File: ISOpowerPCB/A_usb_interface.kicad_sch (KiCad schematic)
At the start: 10 parts, among them J19 USB_B_Mini, U12 CH340C

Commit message: added documentation for component selection
Completed footprint association & added documentation re Netclasses. Need to update netclasses in schematic settings before moving to PCB layout.
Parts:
- J19: footprint (none) -> Connector_USB:USB_Mini-B_Lumberg_2486_01_Horizontal
- TP7, TP8: footprint (none) -> TestPoint:TestPoint_Pad_D1.5mm
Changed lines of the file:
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@@
       (effects (font (size 1.27 1.27)) (justify left))
     )
-    (property "Footprint" "" (id 2) (at 161.29 77.47 0)
+    (property "Footprint" "TestPoint:TestPoint_Pad_D1.5mm" (id 2) (at 161.29 77.47 0)
       (effects (font (size 1.27 1.27)) hide)
     )
@@
       (effects (font (size 1.27 1.27)) (justify left))
     )
-    (property "Footprint" "" (id 2) (at 120.65 77.47 0)
+    (property "Footprint" "TestPoint:TestPoint_Pad_D1.5mm" (id 2) (at 120.65 77.47 0)
       (effects (font (size 1.27 1.27)) hide)
     )
@@
       (effects (font (size 1.27 1.27)) (justify right))
     )
-    (property "Footprint" "" (id 2) (at 177.8 93.98 0)
+    (property "Footprint" "Connector_USB:USB_Mini-B_Lumberg_2486_01_Horizontal" (id 2) (at 177.8 93.98 0)
       (effects (font (size 1.27 1.27)) hide)
     )

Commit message: PCB Layouts
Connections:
- net 5V_CH340 renamed 5V_IN
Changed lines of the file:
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@@
-    (stroke (width 0) (type default) (color 0 0 0 0))
-  )
-  (wire (pts (xy 27.94 22.86) (xy 39.37 22.86))
     (stroke (width 0) (type default) (color 0 0 0 0))
   )
@@
     (stroke (width 0) (type default) (color 0 0 0 0))
   )
-  (wire (pts (xy 27.94 30.48) (xy 39.37 30.48))
-    (stroke (width 0) (type default) (color 0 0 0 0))
-  )
   (wire (pts (xy 115.57 77.47) (xy 119.38 77.47))
     (stroke (width 0) (type default) (color 0 0 0 0))
@@
   )
   (wire (pts (xy 156.21 123.19) (xy 156.21 96.52))
-    (stroke (width 0) (type default) (color 0 0 0 0))
-  )
-  (wire (pts (xy 27.94 26.67) (xy 39.37 26.67))
     (stroke (width 0) (type default) (color 0 0 0 0))
   )
@@
     (effects (font (size 2 2)) (justify left bottom))
   )
-  (label "3V3_BUS" (at 29.21 26.67 0)
-    (effects (font (size 1.27 1.27)) (justify left bottom))
-  )
-  (global_label "5V_CH340" (shape output) (at 39.37 22.86 0) (fields_autoplaced)
+  (hierarchical_label "TxD_A" (shape output) (at 92.71 115.57 180)
+    (effects (font (size 1.27 1.27)) (justify right))
+  )
+  (hierarchical_label "5V_IN" (shape input) (at 132.08 62.23 90)
     (effects (font (size 1.27 1.27)) (justify left))
-    (property "Intersheet References" "${INTERSHEET_REFS}" (id 0) (at 51.2779 22.7806 0)
-      (effects (font (size 1.27 1.27)) (justify left) hide)
-    )
-  )
-  (global_label "3V3_CH340" (shape output) (at 39.37 26.67 0) (fields_autoplaced)
+  )
+  (hierarchical_label "GND" (shape passive) (at 132.08 110.49 270)
+    (effects (font (size 1.27 1.27)) (justify right))
+  )
+  (hierarchical_label "5V_IN" (shape input) (at 113.03 101.6 90)
     (effects (font (size 1.27 1.27)) (justify left))
-    (property "Intersheet References" "${INTERSHEET_REFS}" (id 0) (at 52.4874 26.5906 0)
-      (effects (font (size 1.27 1.27)) (justify left) hide)
-    )
-  )
-  (global_label "5V_CH340" (shape input) (at 132.08 62.23 90) (fields_autoplaced)
-    (effects (font (size 1.27 1.27)) (justify left))
-    (property "Intersheet References" "${INTERSHEET_REFS}" (id 0) (at 132.0006 50.3221 90)
-      (effects (font (size 1.27 1.27)) (justify left) hide)
-    )
-  )
-  (global_label "5V_CH340" (shape input) (at 113.03 101.6 90) (fields_autoplaced)
-    (effects (font (size 1.27 1.27)) (justify left))
-    (property "Intersheet References" "${INTERSHEET_REFS}" (id 0) (at 112.9506 89.6921 90)
-      (effects (font (size 1.27 1.27)) (justify left) hide)
-    )
-  )
-  (hierarchical_label "TxD_A" (shape output) (at 92.71 115.57 180)
-    (effects (font (size 1.27 1.27)) (justify right))
-  )
-  (hierarchical_label "5V_IN" (shape input) (at 27.94 22.86 180)
-    (effects (font (size 1.27 1.27)) (justify right))
   )
   (hierarchical_label "USB_VOUT" (shape output) (at 170.18 87.63 180)
     (effects (font (size 1.27 1.27)) (justify right))
   )
-  (hierarchical_label "3V3_IN" (shape input) (at 27.94 26.67 180)
+  (hierarchical_label "GND" (shape passive) (at 198.12 120.65 270)
     (effects (font (size 1.27 1.27)) (justify right))
   )
@@
     (effects (font (size 1.27 1.27)) (justify right))
   )
-  (hierarchical_label "GND" (shape passive) (at 27.94 30.48 180)
+  (hierarchical_label "GND" (shape passive) (at 113.03 147.32 270)
+    (effects (font (size 1.27 1.27)) (justify right))
+  )
+  (hierarchical_label "GND" (shape passive) (at 181.61 120.65 270)
     (effects (font (size 1.27 1.27)) (justify right))
   )
@@
     (pin "2")
   )
-  (symbol (lib_id "power:GND") (at 181.61 120.65 0) (unit 1)
-    (in_bom yes) (on_board yes) (fields_autoplaced)
-    (property "Reference" "#PWR072" (id 0) (at 181.61 127 0)
-      (effects (font (size 1.27 1.27)) hide)
-    )
-    (property "Value" "GND" (id 1) (at 184.15 121.9199 0)
-      (effects (font (size 1.27 1.27)) (justify left))
-    )
-    (property "Footprint" "" (id 2) (at 181.61 120.65 0)
-      (effects (font (size 1.27 1.27)) hide)
-    )
-    (property "Datasheet" "" (id 3) (at 181.61 120.65 0)
-      (effects (font (size 1.27 1.27)) hide)
-    )
-    (pin "1")
-  )
   (symbol (lib_id "000_Capacitor_Film_Immo:cap_film_0805") (at 121.92 109.22 90) (unit 1)
     (in_bom yes) (on_board yes)
@@
     (pin "4")
   )
-  (symbol (lib_id "power:GND") (at 113.03 147.32 0) (unit 1)
-    (in_bom yes) (on_board yes) (fields_autoplaced)
-    (property "Reference" "#PWR070" (id 0) (at 113.03 153.67 0)
-      (effects (font (size 1.27 1.27)) hide)
-    )
-    (property "Value" "GND" (id 1) (at 115.57 148.5899 0)
-      (effects (font (size 1.27 1.27)) (justify left))
-    )
-    (property "Footprint" "" (id 2) (at 113.03 147.32 0)
-      (effects (font (size 1.27 1.27)) hide)
-    )
-    (property "Datasheet" "" (id 3) (at 113.03 147.32 0)
-      (effects (font (size 1.27 1.27)) hide)
-    )
-    (pin "1")
-  )
-  (symbol (lib_id "power:GND") (at 198.12 120.65 0) (unit 1)
-    (in_bom yes) (on_board yes) (fields_autoplaced)
-    (property "Reference" "#PWR073" (id 0) (at 198.12 127 0)
-      (effects (font (size 1.27 1.27)) hide)
-    )
-    (property "Value" "GND" (id 1) (at 200.66 121.9199 0)
-      (effects (font (size 1.27 1.27)) (justify left))
-    )
-    (property "Footprint" "" (id 2) (at 198.12 120.65 0)
-      (effects (font (size 1.27 1.27)) hide)
-    )
-    (property "Datasheet" "" (id 3) (at 198.12 120.65 0)
-      (effects (font (size 1.27 1.27)) hide)
-    )
-    (pin "1")
-  )
   (symbol (lib_id "000_Resistors_Immo:Resistor_0805") (at 193.04 110.49 0) (unit 1)
     (in_bom yes) (on_board yes)
@@
     (pin "1")
     (pin "2")
-  )
-  (symbol (lib_id "power:GND") (at 132.08 110.49 0) (unit 1)
-    (in_bom yes) (on_board yes) (fields_autoplaced)
-    (property "Reference" "#PWR071" (id 0) (at 132.08 116.84 0)
-      (effects (font (size 1.27 1.27)) hide)
-    )
-    (property "Value" "GND" (id 1) (at 134.62 111.7599 0)
-      (effects (font (size 1.27 1.27)) (justify left))
-    )
-    (property "Footprint" "" (id 2) (at 132.08 110.49 0)
-      (effects (font (size 1.27 1.27)) hide)
-    )
-    (property "Datasheet" "" (id 3) (at 132.08 110.49 0)
-      (effects (font (size 1.27 1.27)) hide)
-    )
-    (pin "1")
   )
   (symbol (lib_id "Connector:TestPoint") (at 115.57 77.47 0) (unit 1)
@@
     (pin "2")
   )
-  (symbol (lib_id "power:GND") (at 39.37 30.48 90) (unit 1)
-    (in_bom yes) (on_board yes) (fields_autoplaced)
-    (property "Reference" "#PWR069" (id 0) (at 45.72 30.48 0)
-      (effects (font (size 1.27 1.27)) hide)
-    )
-    (property "Value" "GND" (id 1) (at 43.18 30.4799 90)
-      (effects (font (size 1.27 1.27)) (justify right))
-    )
-    (property "Footprint" "" (id 2) (at 39.37 30.48 0)
-      (effects (font (size 1.27 1.27)) hide)
-    )
-    (property "Datasheet" "" (id 3) (at 39.37 30.48 0)
-      (effects (font (size 1.27 1.27)) hide)
-    )
-    (pin "1")
-  )
 )

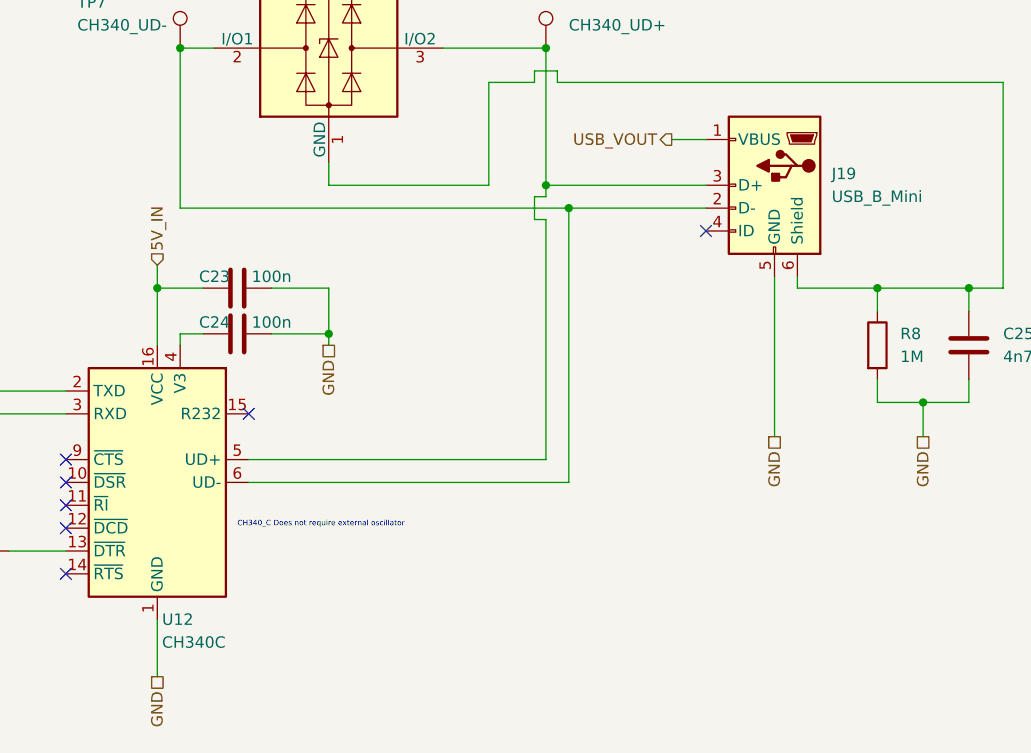
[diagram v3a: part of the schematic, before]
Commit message: Components placed V1.0
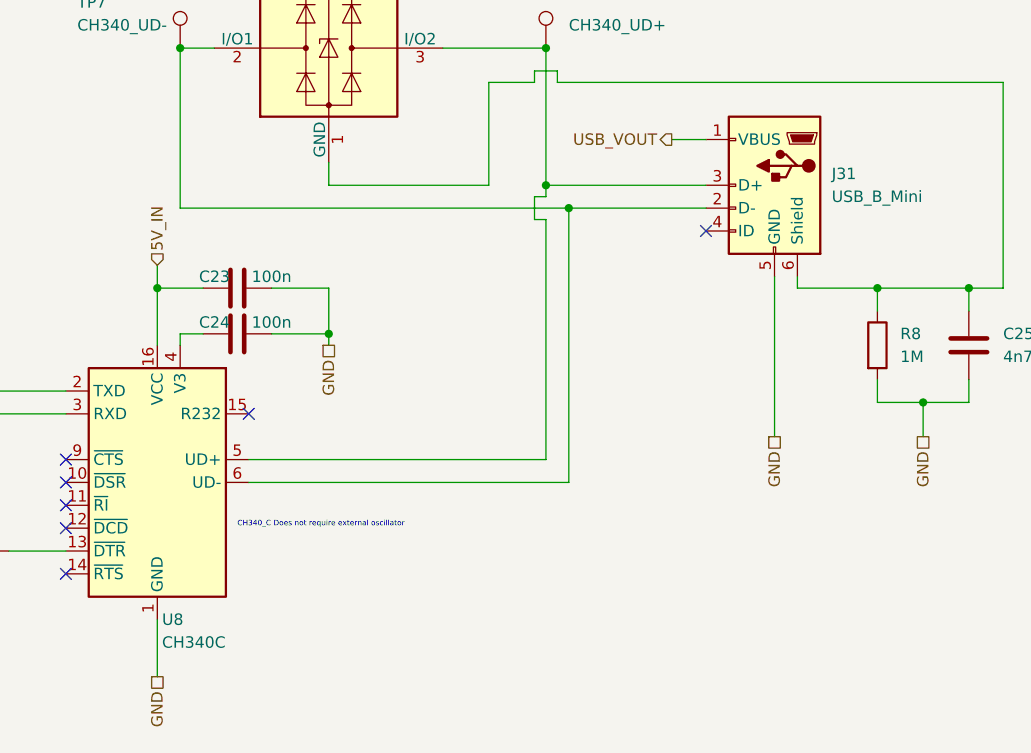
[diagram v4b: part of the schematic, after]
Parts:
- renumbered J19 to J31, U12 to U8
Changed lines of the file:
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@@
   (symbol (lib_id "Connector:USB_B_Mini") (at 181.61 92.71 0) (mirror y) (unit 1)
     (in_bom yes) (on_board yes) (fields_autoplaced)
-    (property "Reference" "J19" (id 0) (at 187.96 91.4399 0)
+    (property "Reference" "J31" (id 0) (at 187.96 91.4399 0)
       (effects (font (size 1.27 1.27)) (justify right))
     )
@@
   (symbol (lib_id "Interface_USB:CH340C") (at 113.03 125.73 0) (mirror y) (unit 1)
     (in_bom yes) (on_board yes) (fields_autoplaced)
-    (property "Reference" "U12" (id 0) (at 113.5506 140.97 0)
+    (property "Reference" "U8" (id 0) (at 113.5506 140.97 0)
       (effects (font (size 1.27 1.27)) (justify right))
     )
